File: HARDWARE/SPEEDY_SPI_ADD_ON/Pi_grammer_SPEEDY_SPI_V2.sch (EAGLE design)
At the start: 11 parts, among them J2 TARGET_copy

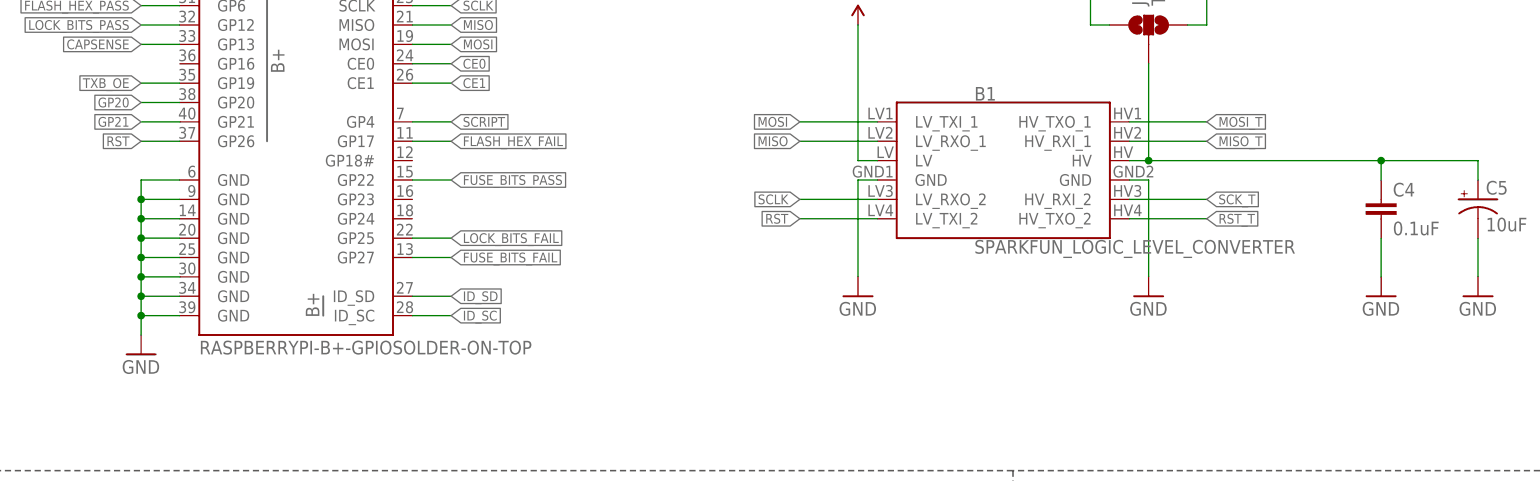
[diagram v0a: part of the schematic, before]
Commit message: SPEED SPI layout work
locking footprint on converter.

moved to 16 mils traces everywhere.

curved traces to keep length of data lines as similar as possible.

removed pin 20 GND on PI header. Not necessary and wanted more clearance
from nearby data trace.
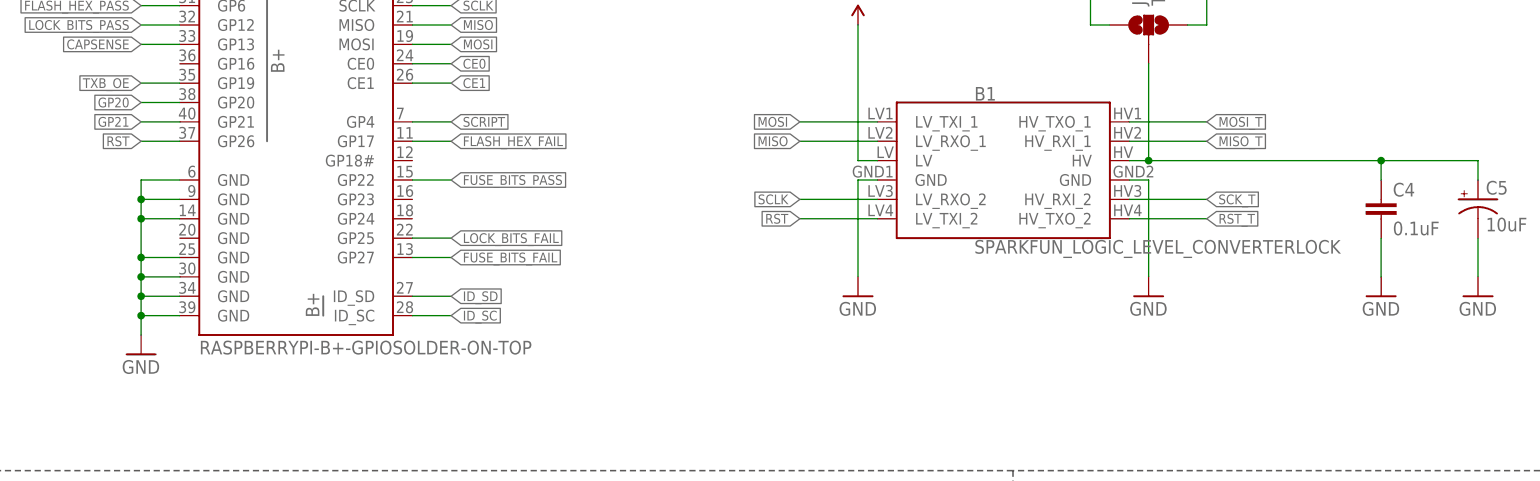
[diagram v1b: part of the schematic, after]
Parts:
- B1: value SPARKFUN_LOGIC_LEVEL_CONVERTER -> SPARKFUN_LOGIC_LEVEL_CONVERTERLOCK; device SparkFun-Boards:SPARKFUN_LOGIC_LEVEL_CONVERTER -> SparkFun-Boards:SPARKFUN_LOGIC_LEVEL_CONVERTERLOCK
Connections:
- net GND: no longer JP2.GND@20
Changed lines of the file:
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@@
 <grid distance="0.1" unitdist="inch" unit="inch" style="lines" multiple="1" display="no" altdistance="0.01" altunitdist="inch" altunit="inch"/>
 <layers>
-<layer number="1" name="Top" color="4" fill="1" visible="yes" active="no"/>
-<layer number="2" name="Route2" color="1" fill="3" visible="yes" active="no"/>
-<layer number="3" name="Route3" color="4" fill="3" visible="yes" active="no"/>
-<layer number="4" name="Route4" color="1" fill="4" visible="yes" active="no"/>
-<layer number="5" name="Route5" color="4" fill="4" visible="yes" active="no"/>
-<layer number="6" name="Route6" color="1" fill="8" visible="yes" active="no"/>
-<layer number="7" name="Route7" color="4" fill="8" visible="yes" active="no"/>
-<layer number="8" name="Route8" color="1" fill="2" visible="yes" active="no"/>
-<layer number="9" name="Route9" color="4" fill="2" visible="yes" active="no"/>
-<layer number="10" name="Route10" color="1" fill="7" visible="yes" active="no"/>
-<layer number="11" name="Route11" color="4" fill="7" visible="yes" active="no"/>
-<layer number="12" name="Route12" color="1" fill="5" visible="yes" active="no"/>
-<layer number="13" name="Route13" color="4" fill="5" visible="yes" active="no"/>
-<layer number="14" name="Route14" color="1" fill="6" visible="yes" active="no"/>
-<layer number="15" name="Route15" color="4" fill="6" visible="yes" active="no"/>
-<layer number="16" name="Bottom" color="1" fill="1" visible="yes" active="no"/>
-<layer number="17" name="Pads" color="2" fill="1" visible="yes" active="no"/>
-<layer number="18" name="Vias" color="2" fill="1" visible="yes" active="no"/>
-<layer number="19" name="Unrouted" color="6" fill="1" visible="yes" active="no"/>
-<layer number="20" name="Dimension" color="15" fill="1" visible="yes" active="no"/>
-<layer number="21" name="tPlace" color="16" fill="1" visible="yes" active="no"/>
-<layer number="22" name="bPlace" color="14" fill="1" visible="yes" active="no"/>
-<layer number="23" name="tOrigins" color="15" fill="1" visible="yes" active="no"/>
-<layer number="24" name="bOrigins" color="15" fill="1" visible="yes" active="no"/>
-<layer number="25" name="tNames" color="7" fill="1" visible="yes" active="no"/>
-<layer number="26" name="bNames" color="7" fill="1" visible="yes" active="no"/>
-<layer number="27" name="tValues" color="7" fill="1" visible="yes" active="no"/>
-<layer number="28" name="bValues" color="7" fill="1" visible="yes" active="no"/>
+<layer number="1" name="Top" color="4" fill="1" visible="no" active="no"/>
+<layer number="2" name="Route2" color="1" fill="3" visible="no" active="no"/>
+<layer number="3" name="Route3" color="4" fill="3" visible="no" active="no"/>
+<layer number="4" name="Route4" color="1" fill="4" visible="no" active="no"/>
+<layer number="5" name="Route5" color="4" fill="4" visible="no" active="no"/>
+<layer number="6" name="Route6" color="1" fill="8" visible="no" active="no"/>
+<layer number="7" name="Route7" color="4" fill="8" visible="no" active="no"/>
+<layer number="8" name="Route8" color="1" fill="2" visible="no" active="no"/>
+<layer number="9" name="Route9" color="4" fill="2" visible="no" active="no"/>
+<layer number="10" name="Route10" color="1" fill="7" visible="no" active="no"/>
+<layer number="11" name="Route11" color="4" fill="7" visible="no" active="no"/>
+<layer number="12" name="Route12" color="1" fill="5" visible="no" active="no"/>
+<layer number="13" name="Route13" color="4" fill="5" visible="no" active="no"/>
+<layer number="14" name="Route14" color="1" fill="6" visible="no" active="no"/>
+<layer number="15" name="Route15" color="4" fill="6" visible="no" active="no"/>
+<layer number="16" name="Bottom" color="1" fill="1" visible="no" active="no"/>
+<layer number="17" name="Pads" color="2" fill="1" visible="no" active="no"/>
+<layer number="18" name="Vias" color="2" fill="1" visible="no" active="no"/>
+<layer number="19" name="Unrouted" color="6" fill="1" visible="no" active="no"/>
+<layer number="20" name="Dimension" color="15" fill="1" visible="no" active="no"/>
+<layer number="21" name="tPlace" color="16" fill="1" visible="no" active="no"/>
+<layer number="22" name="bPlace" color="14" fill="1" visible="no" active="no"/>
+<layer number="23" name="tOrigins" color="15" fill="1" visible="no" active="no"/>
+<layer number="24" name="bOrigins" color="15" fill="1" visible="no" active="no"/>
+<layer number="25" name="tNames" color="7" fill="1" visible="no" active="no"/>
+<layer number="26" name="bNames" color="7" fill="1" visible="no" active="no"/>
+<layer number="27" name="tValues" color="7" fill="1" visible="no" active="no"/>
+<layer number="28" name="bValues" color="7" fill="1" visible="no" active="no"/>
 <layer number="29" name="tStop" color="7" fill="3" visible="no" active="no"/>
 <layer number="30" name="bStop" color="7" fill="6" visible="no" active="no"/>
@@
 <layer number="35" name="tGlue" color="7" fill="4" visible="no" active="no"/>
 <layer number="36" name="bGlue" color="7" fill="5" visible="no" active="no"/>
-<layer number="37" name="tTest" color="7" fill="1" visible="yes" active="no"/>
-<layer number="38" name="bTest" color="7" fill="1" visible="yes" active="no"/>
+<layer number="37" name="tTest" color="7" fill="1" visible="no" active="no"/>
+<layer number="38" name="bTest" color="7" fill="1" visible="no" active="no"/>
 <layer number="39" name="tKeepout" color="4" fill="11" visible="no" active="no"/>
 <layer number="40" name="bKeepout" color="1" fill="11" visible="no" active="no"/>
@@
 <layer number="44" name="Drills" color="7" fill="1" visible="no" active="no"/>
 <layer number="45" name="Holes" color="7" fill="1" visible="no" active="no"/>
-<layer number="46" name="Milling" color="3" fill="1" visible="yes" active="no"/>
-<layer number="47" name="Measures" color="7" fill="1" visible="yes" active="no"/>
-<layer number="48" name="Document" color="7" fill="1" visible="yes" active="no"/>
-<layer number="49" name="Reference" color="13" fill="1" visible="yes" active="no"/>
-<layer number="50" name="dxf" color="7" fill="1" visible="yes" active="no"/>
-<layer number="51" name="tDocu" color="6" fill="1" visible="yes" active="no"/>
-<layer number="52" name="bDocu" color="7" fill="1" visible="yes" active="no"/>
-<layer number="53" name="tGND_GNDA" color="7" fill="9" visible="yes" active="no"/>
-<layer number="54" name="bGND_GNDA" color="1" fill="9" visible="yes" active="no"/>
-<layer number="56" name="wert" color="7" fill="1" visible="yes" active="no"/>
-<layer number="57" name="tCAD" color="7" fill="1" visible="yes" active="no"/>
-<layer number="59" name="tCarbon" color="7" fill="1" visible="yes" active="no"/>
-<layer number="60" name="bCarbon" color="7" fill="1" visible="yes" active="no"/>
+<layer number="46" name="Milling" color="3" fill="1" visible="no" active="no"/>
+<layer number="47" name="Measures" color="7" fill="1" visible="no" active="no"/>
+<layer number="48" name="Document" color="7" fill="1" visible="no" active="no"/>
+<layer number="49" name="Reference" color="13" fill="1" visible="no" active="no"/>
+<layer number="50" name="dxf" color="7" fill="1" visible="no" active="no"/>
+<layer number="51" name="tDocu" color="6" fill="1" visible="no" active="no"/>
+<layer number="52" name="bDocu" color="7" fill="1" visible="no" active="no"/>
+<layer number="53" name="tGND_GNDA" color="7" fill="9" visible="no" active="no"/>
+<layer number="54" name="bGND_GNDA" color="1" fill="9" visible="no" active="no"/>
+<layer number="56" name="wert" color="7" fill="1" visible="no" active="no"/>
+<layer number="57" name="tCAD" color="7" fill="1" visible="no" active="no"/>
+<layer number="59" name="tCarbon" color="7" fill="1" visible="no" active="no"/>
+<layer number="60" name="bCarbon" color="7" fill="1" visible="no" active="no"/>
 <layer number="90" name="Modules" color="5" fill="1" visible="yes" active="yes"/>
 <layer number="91" name="Nets" color="2" fill="1" visible="yes" active="yes"/>
@@
 <part name="GND6" library="SparkFun-Aesthetics" deviceset="GND" device=""/>
 <part name="FRAME1" library="SparkFun-Aesthetics" deviceset="FRAME-LETTER" device=""/>
-<part name="B1" library="SparkFun-Boards" deviceset="SPARKFUN_LOGIC_LEVEL_CONVERTER" device=""/>
+<part name="B1" library="SparkFun-Boards" deviceset="SPARKFUN_LOGIC_LEVEL_CONVERTER" device="LOCK" value="SPARKFUN_LOGIC_LEVEL_CONVERTERLOCK"/>
 <part name="GND4" library="SparkFun-Aesthetics" deviceset="GND" device=""/>
 <part name="GND5" library="SparkFun-Aesthetics" deviceset="GND" device=""/>
@@
 <wire x1="40.64" y1="289.56" x2="40.64" y2="292.1" width="0.1524" layer="91"/>
 <wire x1="40.64" y1="292.1" x2="40.64" y2="294.64" width="0.1524" layer="91"/>
-<wire x1="40.64" y1="294.64" x2="40.64" y2="297.18" width="0.1524" layer="91"/>
-<wire x1="40.64" y1="297.18" x2="40.64" y2="299.72" width="0.1524" layer="91"/>
+<wire x1="40.64" y1="294.64" x2="40.64" y2="299.72" width="0.1524" layer="91"/>
 <wire x1="40.64" y1="299.72" x2="40.64" y2="302.26" width="0.1524" layer="91"/>
 <wire x1="40.64" y1="302.26" x2="40.64" y2="304.8" width="0.1524" layer="91"/>
@@
 <pinref part="JP2" gate="G$1" pin="GND@14"/>
 <wire x1="45.72" y1="299.72" x2="40.64" y2="299.72" width="0.1524" layer="91"/>
-<pinref part="JP2" gate="G$1" pin="GND@20"/>
-<wire x1="45.72" y1="297.18" x2="40.64" y2="297.18" width="0.1524" layer="91"/>
 <pinref part="JP2" gate="G$1" pin="GND@25"/>
 <wire x1="45.72" y1="294.64" x2="40.64" y2="294.64" width="0.1524" layer="91"/>
@@
 <junction x="40.64" y="292.1"/>
 <junction x="40.64" y="294.64"/>
-<junction x="40.64" y="297.18"/>
 <junction x="40.64" y="299.72"/>
 <junction x="40.64" y="302.26"/>
